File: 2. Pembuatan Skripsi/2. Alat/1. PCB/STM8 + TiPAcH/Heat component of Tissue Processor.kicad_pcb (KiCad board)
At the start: 2 copper layers, 42 x 62.1 mm, 57 parts, among them J1 Conn_01x02, J2 Sensors, J3 Screw_Terminal_01x02, J8 Conn_01x06, K1 EE2-4.5NU, Q1 S9013, Q2 S9013, Q3 S9013, Q4 MMBT2222, SW1 SW_SPST, SW2 SW_SPST, SW3 SW_SPST, U2 AP2112K-3.3, U6 STM8L051F3P, Y1 32.768KHz

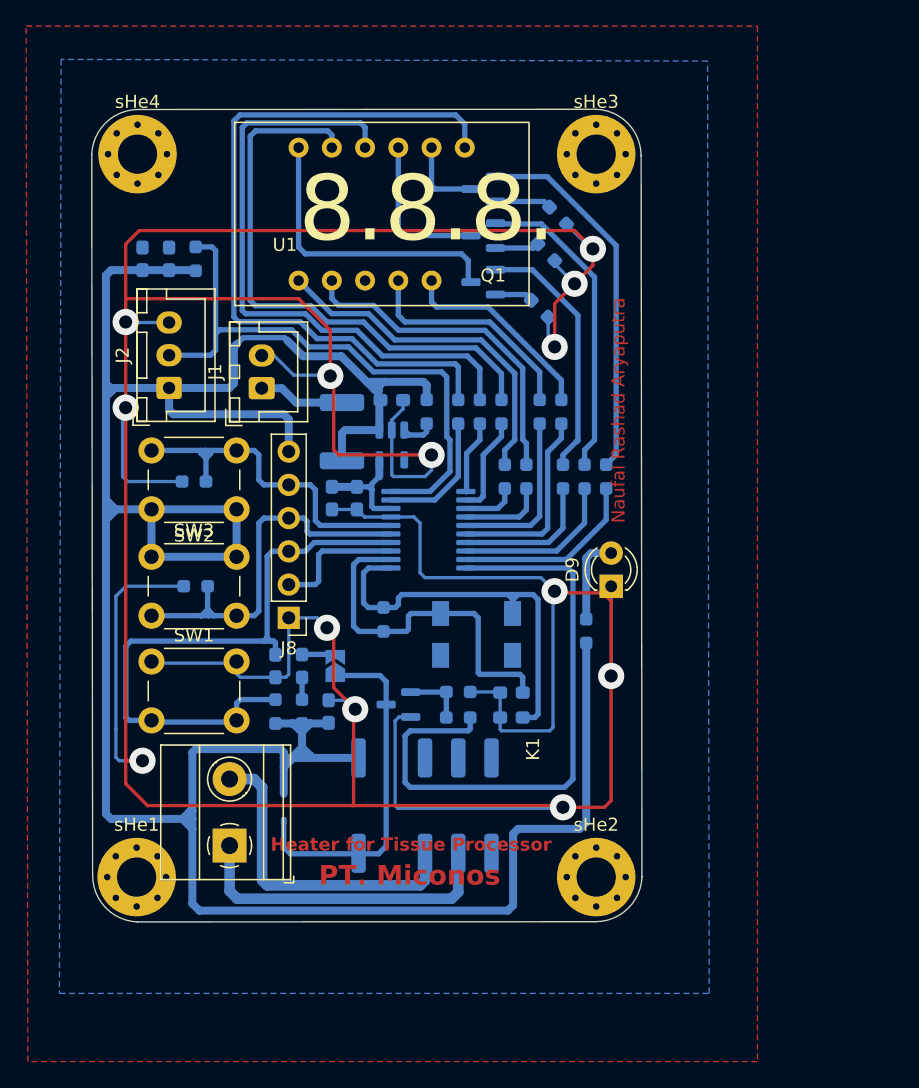
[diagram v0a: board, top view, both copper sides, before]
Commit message: *Major Update*
- STM8S PCB jumpers are relocated to make it easier to solder it
- ATMEGA328 version is added and revised for backup option
- Arduino Code for ATMEGA328 is added.
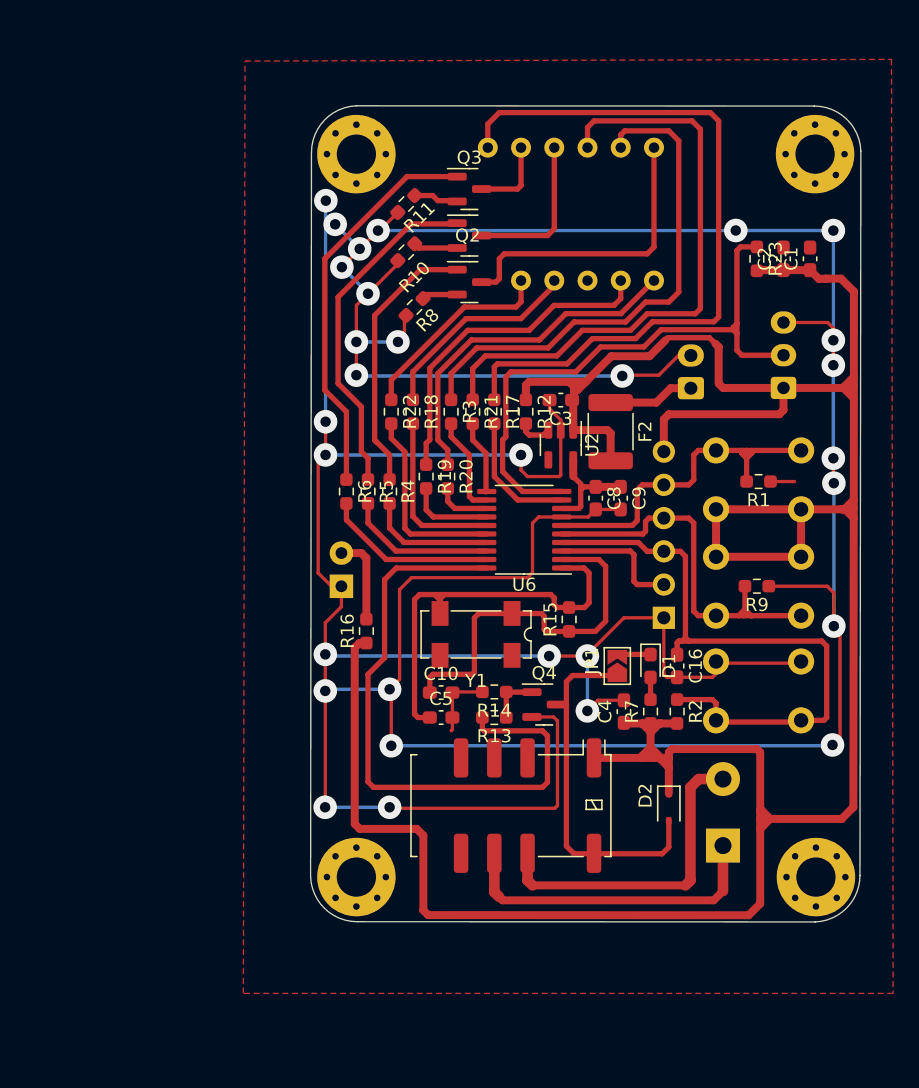
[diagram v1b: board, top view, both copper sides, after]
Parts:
- C1, C10, C16, C2, C3, C4, C5, C8, C9, D1, D2, F2, JP1, K1, Q1, Q2, Q3, Q4, R1, R10, R11, R12, R13, R14, R15, R16, R17, R18, R19, R2, R20, R21, R22, R23, R3, R4, R5, R6, R7, R8, R9, U2, U6, Y1: moved to F.Cu
- D9, J1, J2, J3, J8, SW1, SW2, SW3, U1, sHe1, sHe2, sHe3, sHe4: moved to B.Cu
- moved sHe1 51.9 mm to (70.5, 125.9), turned to 180 degrees
- moved sHe4 51.8 mm to (70.4, 70.6), turned to 180 degrees
- moved C1 51.0 mm to (70.1, 78.6)
- moved SW1 49.6 mm to (69.4, 109.4), turned to 180 degrees
- moved SW3 49.6 mm to (69.4, 101.4), turned to 180 degrees
- moved C2 47.0 mm to (68.0, 78.6)
- moved J2 47.0 mm to (68.0, 88.5)
- moved R1 43.1 mm to (66.1, 95.6), turned to 180 degrees
- moved R23 42.9 mm to (66.0, 78.6)
- moved R9 42.9 mm to (66.0, 103.6), turned to 180 degrees
- moved J3 37.7 mm to (63.4, 123.4)
- moved SW2 36.6 mm to (62.9, 97.8), turned to 0 degrees
- moved J1 32.8 mm to (61.0, 88.5)
- moved C16 30.7 mm to (59.9, 109.7)
- moved R2 30.7 mm to (59.9, 113.2)
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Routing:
- net GND: track 343.2 -> 372.0 mm, vias 13 -> 30
- net a: track 43.6 -> 39.4 mm
- net VCC: track 229.5 -> 233.2 mm
- net Net-(Q2-B): track 23.9 -> 26.3 mm
- net Net-(Q3-B): track 28.5 -> 30.3 mm
- net f: track 47.6 -> 46.0 mm
- net c: track 17.4 -> 16.0 mm
- net EN2: track 12.6 -> 11.5 mm
- net Net-(Q1-B): track 19.6 -> 20.8 mm
- net EN1: track 10.9 -> 9.76 mm
- net EN3: track 14.4 -> 13.2 mm
- net Net-(Q3-E): track 4.31 -> 3.43 mm
- net RELAYPIN: track 47.0 -> 47.8 mm
- net OSCOUT: track 27.6 -> 28.3 mm
- net Temp: track 44.7 -> 45.3 mm
- removed copper zone on B.Cu, net GND
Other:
- board size 42 x 62.1 mm -> 42 x 62.4 mm
- board text removed: "Heater for Tissue Processor"
- board text removed: "Naufal Rashad Aryaputra"
- board text removed: "PT. Miconos"
